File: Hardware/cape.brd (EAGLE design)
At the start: 118.2 x 97.2 mm, 48 parts, among them IC1 RT7258, IC3 74HC125, IC4 74VHC541, IC5 74VHC541, J1 FCI-10118064-5001310LF, J2 FCI-10118064-5001310LF, Q1 FDS6670, X1 RJ45-6L2-B, X2 RJ45-6L2-B

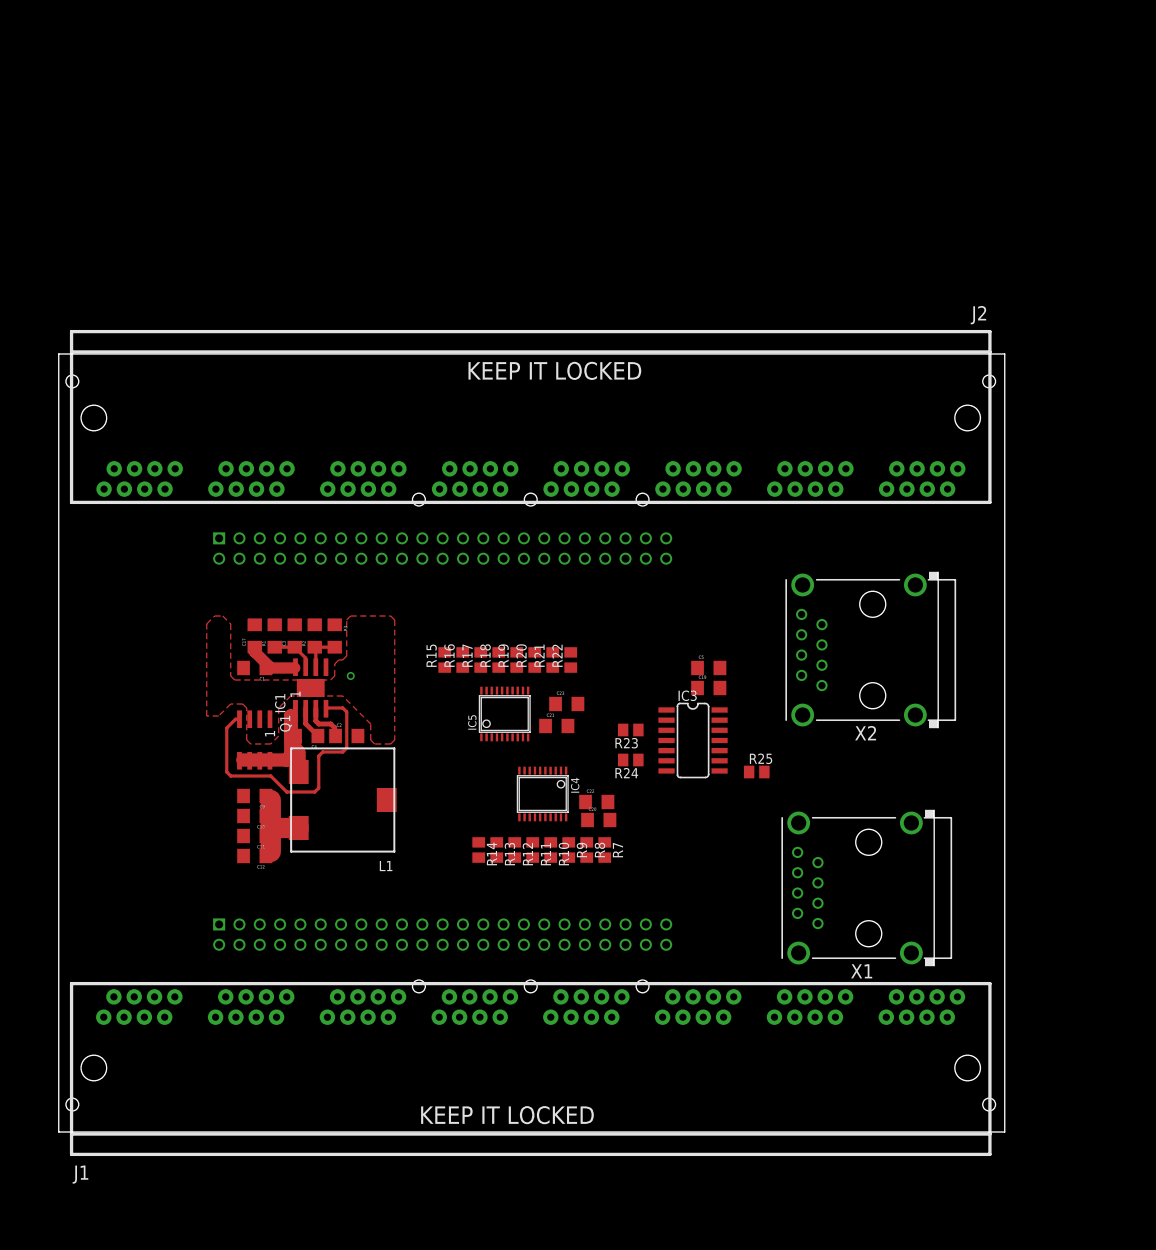
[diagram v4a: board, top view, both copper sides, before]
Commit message: Working on board routing
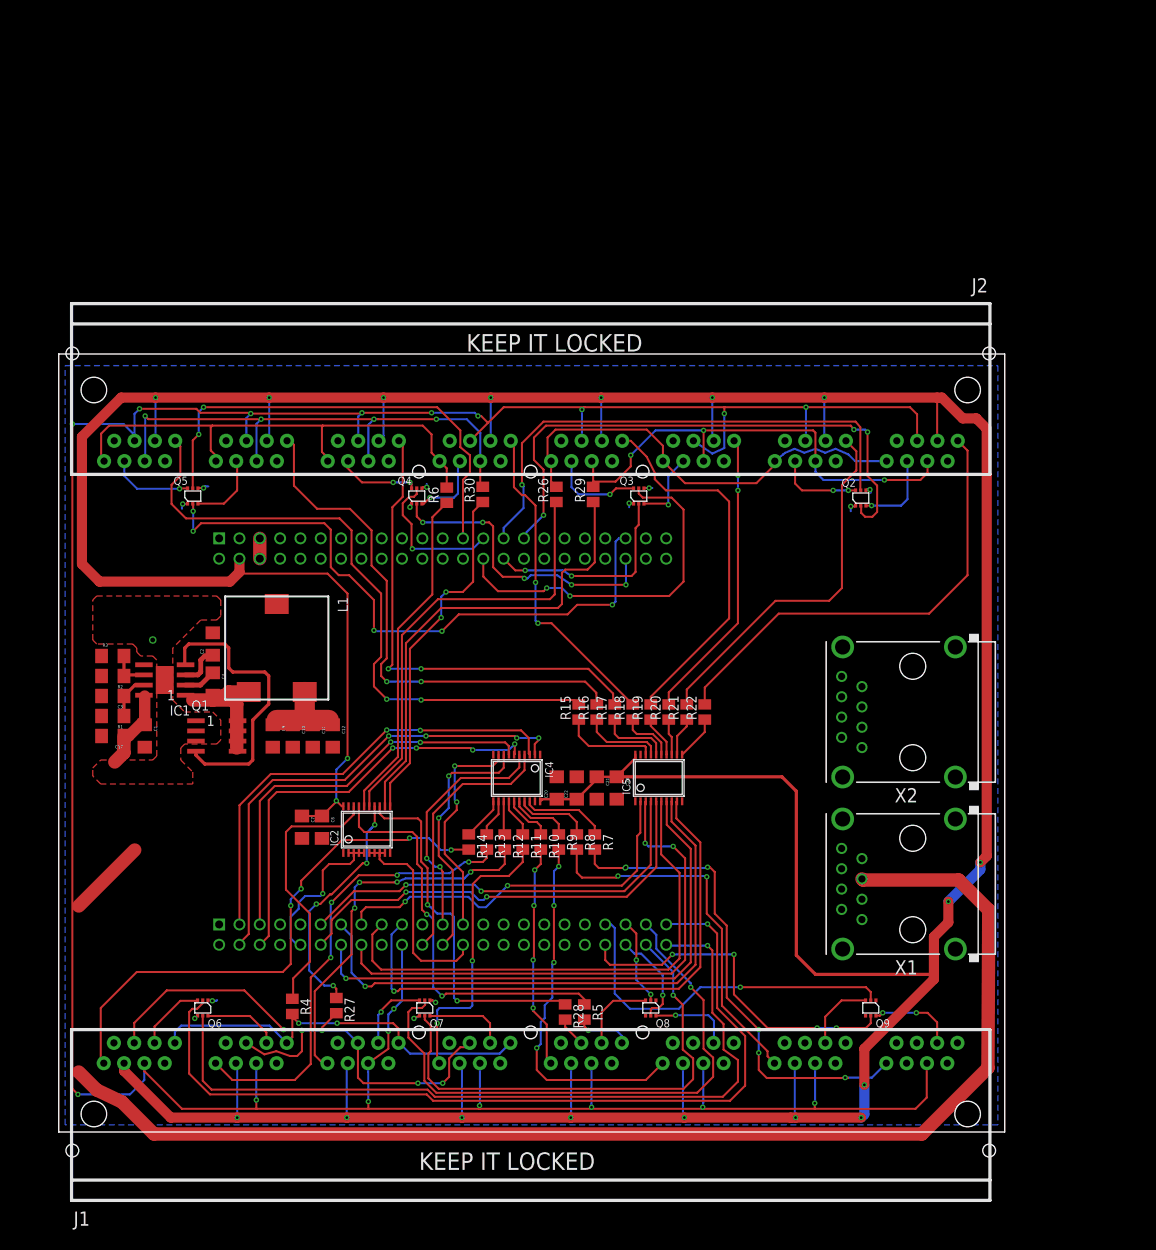
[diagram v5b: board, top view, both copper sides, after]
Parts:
- removed C19: 1uF, SparkFun-Capacitors:1206
- removed C5: 10uF, SparkFun-Capacitors:1206
- removed IC3: 74HC125, TotU:SOIC-14
- removed R23, R24, R25: (no value), resistor:M0805
- added C6: 1uF, SparkFun-Capacitors:1206
- added C7: 10uF, SparkFun-Capacitors:1206
- added IC2: 74VHC541, cape:TSSOP20
- added Q2, Q3, Q4, Q5, Q6, Q7, Q8, Q9: N-MOSFET-DUAL, cape:TSSOP6
- added R26, R27, R28, R29, R30, R4, R5, R6: (no value), resistor:M0805
- moved R3 27.9 mm to (6.75, 40.0), turned to 0 degrees
- moved R2 25.7 mm to (6.75, 37.5), turned to 180 degrees
- moved C3 24.0 mm to (6.75, 35.0), turned to 180 degrees
- moved R1 22.6 mm to (6.75, 32.5), turned to 180 degrees
- moved C17 21.7 mm to (6.75, 30.0), turned to 180 degrees
- moved IC5 20.8 mm to (75.0, 24.8)
- moved L1 20.7 mm to (27.2, 41.0), turned to 270 degrees
- moved C2 20.3 mm to (19.2, 41.5), turned to 90 degrees
- moved IC1 18.3 mm to (13.2, 37.0), turned to 90 degrees
- moved R15 18.0 mm to (65.0, 33.0)
- moved R16 18.0 mm to (67.2, 33.0)
- moved R17 18.0 mm to (69.5, 33.0)
- moved R18 18.0 mm to (71.8, 33.0)
- moved R19 18.0 mm to (74.0, 33.0)
- moved R20 18.0 mm to (76.2, 33.0)
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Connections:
- removed net BKL0: J1.A6
- removed net BLK1: J1.B6
- removed net BLK10: J2.C6
- removed net BLK11: J2.D6
- removed net BLK12: J2.E6
- removed net BLK13: J2.F6
- removed net BLK14: J2.G6
- removed net BLK15: J2.H6
- removed net BLK2: J1.C6
- removed net BLK3: J1.D6
- removed net BLK4: J1.E6
- removed net BLK5: J1.F6
- removed net BLK6: J1.G6
- removed net BLK7: J1.H6
- removed net BLK8: J2.A6
- removed net BLK9: J2.B6
- removed net DC: J1.A4, J1.B4, J1.C4, J1.D4, J1.E4, J1.F4, J1.G4, J1.H4, J2.A4, J2.B4, J2.C4, J2.D4, J2.E4, J2.F4, J2.G4, J2.H4, R24.2
- removed net N$29: IC3.8, R25.1
- removed net N$30: IC3.6, R24.1
- removed net N$31: IC3.3, R23.1
- removed net RST_RAW: IC3.9, U$1.20
- removed net SCK: J1.A8, J1.B8, J1.C8, J1.D8, J1.E8, J1.F8, J1.G8, J1.H8, J2.A8, J2.B8, J2.C8, J2.D8, J2.E8, J2.F8, J2.G8, J2.H8, R23.2
- removed net VDD_5V: U$1.52
- new net BL0: J1.A6, Q6.3
- new net BL1: J1.B6, Q6.6
- new net BL10: J2.C6, Q3.3
- new net BL11: J2.D6, Q3.6
- new net BL12: J2.E6, Q4.3
- new net BL13: J2.F6, Q4.6
- new net BL14: J2.G6, Q5.3
- new net BL15: J2.H6, Q5.6
- new net BL2: J1.C6, Q7.3
- new net BL3: J1.D6, Q7.6
- new net BL4: J1.E6, Q8.3
- new net BL5: J1.F6, Q8.6
- new net BL6: J1.G6, Q9.3
- new net BL7: J1.H6, Q9.6
- new net BL8: J2.A6, Q2.3
- new net BL9: J2.B6, Q2.6
- new net DC0: J1.A4, J1.B4, J1.C4, J1.D4, R27.2
- new net DC1: J1.E4, J1.F4, J1.G4, J1.H4, R28.2
- new net DC2: J2.A4, J2.B4, J2.C4, J2.D4, R29.2
- new net DC3: J2.E4, J2.F4, J2.G4, J2.H4, R30.2
- new net N$10: IC2.17, R5.1
- new net N$11: IC2.16, R6.1
- new net N$12: IC2.15, R26.1
- new net N$14: IC2.14, R27.1
- new net N$15: IC2.13, R28.1
- new net N$32: IC2.12, R29.1
- new net N$33: IC2.11, R30.1
- new net N$9: IC2.18, R4.1
- new net PRU0-0: Q2.2, U$1.77
- new net PRU0-1: Q2.5, U$1.75
- new net PRU0-2: Q3.2, U$1.76
- new net PRU0-3: Q3.5, U$1.74
- new net PRU0-4: Q4.2, U$1.88
- new net PRU0-5: Q4.5, U$1.73
- new net PRU0-6: Q5.2, U$1.87
- new net PRU0-7: Q5.5, U$1.71
- new net PRU1-0: Q6.2, U$1.45
- new net PRU1-1: Q6.5, U$1.46
- new net PRU1-10: U$1.28
- new net PRU1-12: U$1.21
- new net PRU1-2: Q7.2, U$1.43
- new net PRU1-3: Q7.5, U$1.44
- new net PRU1-4: Q8.2, U$1.41
- new net PRU1-5: Q8.5, U$1.42
- new net PRU1-6: Q9.2, U$1.39
- new net PRU1-7: Q9.5, U$1.40
- new net PRU1-8: U$1.27
- new net PRU1-9: U$1.29
- new net SCK0: J1.A8, J1.B8, J1.C8, J1.D8, R4.2
- new net SCK1: J1.E8, J1.F8, J1.G8, J1.H8, R5.2
- new net SCK2: J2.A8, J2.B8, J2.C8, J2.D8, R26.2
- new net SCK3: J2.E8, J2.F8, J2.G8, J2.H8, R6.2
- net DC_RAW: now also IC2.6, IC2.7, IC2.8, IC2.9; no longer IC3.5
- net GND: now also C6.2, C7.2, IC2.1, IC2.10, IC2.19, Q2.1, Q2.4, Q3.1, Q3.4, Q4.1, Q4.4, Q5.1, Q5.4, Q6.1, Q6.4, Q7.1, Q7.4, Q8.1, Q8.4, Q9.1, Q9.4; no longer C19.1, C5.1, IC3.1, IC3.10, IC3.12, IC3.13, IC3.4, IC3.7
- net RST: now also U$1.20; no longer R25.2
- net SCL_RAW: now also IC2.2, IC2.3, IC2.4, IC2.5; no longer IC3.2
- net VCC3V3: now also C6.1, C7.1, IC2.20; no longer C19.2, C5.2, IC3.14
- net VCC5V: now also U$1.52
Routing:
- net VCC3V3: track 0.00 -> 552.8 mm, vias 0 -> 19
- net RST: track 0.00 -> 396.5 mm, vias 0 -> 18
- net VIN: track 8.54 -> 179.4 mm
- net PRU1-0: track 0.00 -> 109.2 mm, vias 0 -> 1
- net PRU1-1: track 0.00 -> 100.6 mm, vias 0 -> 1
- net DATA15: track 0.00 -> 80.4 mm, vias 0 -> 2
- net PRU0-6: track 0.00 -> 77.7 mm, vias 0 -> 5
- net AD9: track 0.00 -> 73.1 mm, vias 0 -> 1
- net PRU1-2: track 0.00 -> 72.7 mm, vias 0 -> 1
- net PRU0-0: track 0.00 -> 70.7 mm, vias 0 -> 3
- net AD8: track 0.00 -> 70.6 mm, vias 0 -> 1
- net DC0: track 0.00 -> 70.2 mm, vias 0 -> 5
- net AD10: track 0.00 -> 69.8 mm, vias 0 -> 1
- net DATA0: track 0.00 -> 67.8 mm, vias 0 -> 4
- net AD14: track 0.00 -> 67.8 mm, vias 0 -> 2
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- added copper zone on layer 16, net GND

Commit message: Routing
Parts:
- removed X1, X2: RJ45-6L2-B, con-tycoelectronics:RJ45-SHIELD2
- added J3, J4: RJ45-8P8C, cape:54602-908LF
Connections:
- removed net RX+: X1.3, X2.3
- removed net RX-: X1.6, X2.6
- removed net TX+: X1.1, X2.1
- removed net TX-: X1.2, X2.2
- new net RX_N: J3.6, J4.6
- new net RX_P: J3.3, J4.3
- new net TX_N: J3.2, J4.2
- new net TX_P: J3.1, J4.1
- net GND: now also J3.7, J3.8; no longer X1.7, X1.8, X1.S1, X1.S2, X1.S3, X1.S4, X2.S1, X2.S2, X2.S3, X2.S4
- net VIN: now also J3.4, J3.5; no longer X1.4, X1.5
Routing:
- net DC1: track 3.74 -> 62.4 mm, vias 0 -> 2
- net VCC5V: track 18.5 -> 75.3 mm, vias 0 -> 3
- net GND: track 13.0 -> 68.8 mm, vias 13 -> 231
- net SCK1: track 6.91 -> 55.9 mm, vias 1 -> 2
- net TX_P: track 0.00 -> 37.4 mm
- net VIN: track 179.4 -> 212.7 mm, vias 0 -> 1
- net RX_N: track 0.00 -> 30.4 mm
- net TX_N: track 0.00 -> 29.6 mm
- net RX_P: track 0.00 -> 27.1 mm
- net VCC3V3: track 552.8 -> 561.5 mm
- net DC0: track 70.2 -> 67.3 mm, vias 5 -> 4
- net DATA7: track 62.3 -> 61.6 mm, vias 6 -> 5
- net N$4: track 21.8 -> 22.3 mm
- net BL5: track 10.3 -> 10.1 mm, vias 1 -> 2
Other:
- board size 118.2 x 97.2 mm -> 118.2 x 103.5 mm

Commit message: Finished v1 board
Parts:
- added 3V, 5V, GND, PRU1-10, PRU1-12, PRU1-8, PRU1-9, VIN: PTR1TP20R, tenna_avr_AD7021_v0_9_shrink:TP20R
- added F1: PTC, cape:LF-1812L
- added U$2, U$3: (no value), holes:3,2
- added U$4, U$5, U$6: FIDUCIAL, adafruit:FIDUCIAL_1MM
- L1: value MURATA_INDUCTOR_3900 -> 2.8uH
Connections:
- new net VFUSE: C1.1, C17.1, F1.P$1C, IC1.8, R1.2
- net GND: now also GND.TP
- net PRU1-10: now also PRU1-10.TP
- net PRU1-12: now also PRU1-12.TP
- net PRU1-8: now also PRU1-8.TP
- net PRU1-9: now also PRU1-9.TP
- net VCC3V3: now also 3V.TP
- net VCC5V: now also 5V.TP
- net VIN: now also F1.P$2, VIN.TP; no longer C1.1, C17.1, IC1.8, R1.2
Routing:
- net VIN: track 212.7 -> 174.4 mm
- net VFUSE: track 0.00 -> 37.8 mm
- net VCC5V: track 75.3 -> 94.2 mm
- net PRU1-12: track 0.00 -> 10.2 mm
- net PRU1-9: track 0.00 -> 4.78 mm
- net PRU1-8: track 0.00 -> 3.89 mm
- net DATA0: track 67.8 -> 71.3 mm
- net PRU1-10: track 0.00 -> 3.26 mm
- net VCC3V3: track 561.5 -> 564.1 mm
- net GND: track 68.8 -> 70.4 mm
- net DC0: track 67.3 -> 65.8 mm
- net AD13: track 52.9 -> 54.0 mm
- net AD15: track 48.1 -> 49.0 mm
- net DATA4: track 28.0 -> 28.7 mm
- net BL0: track 8.77 -> 8.06 mm
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
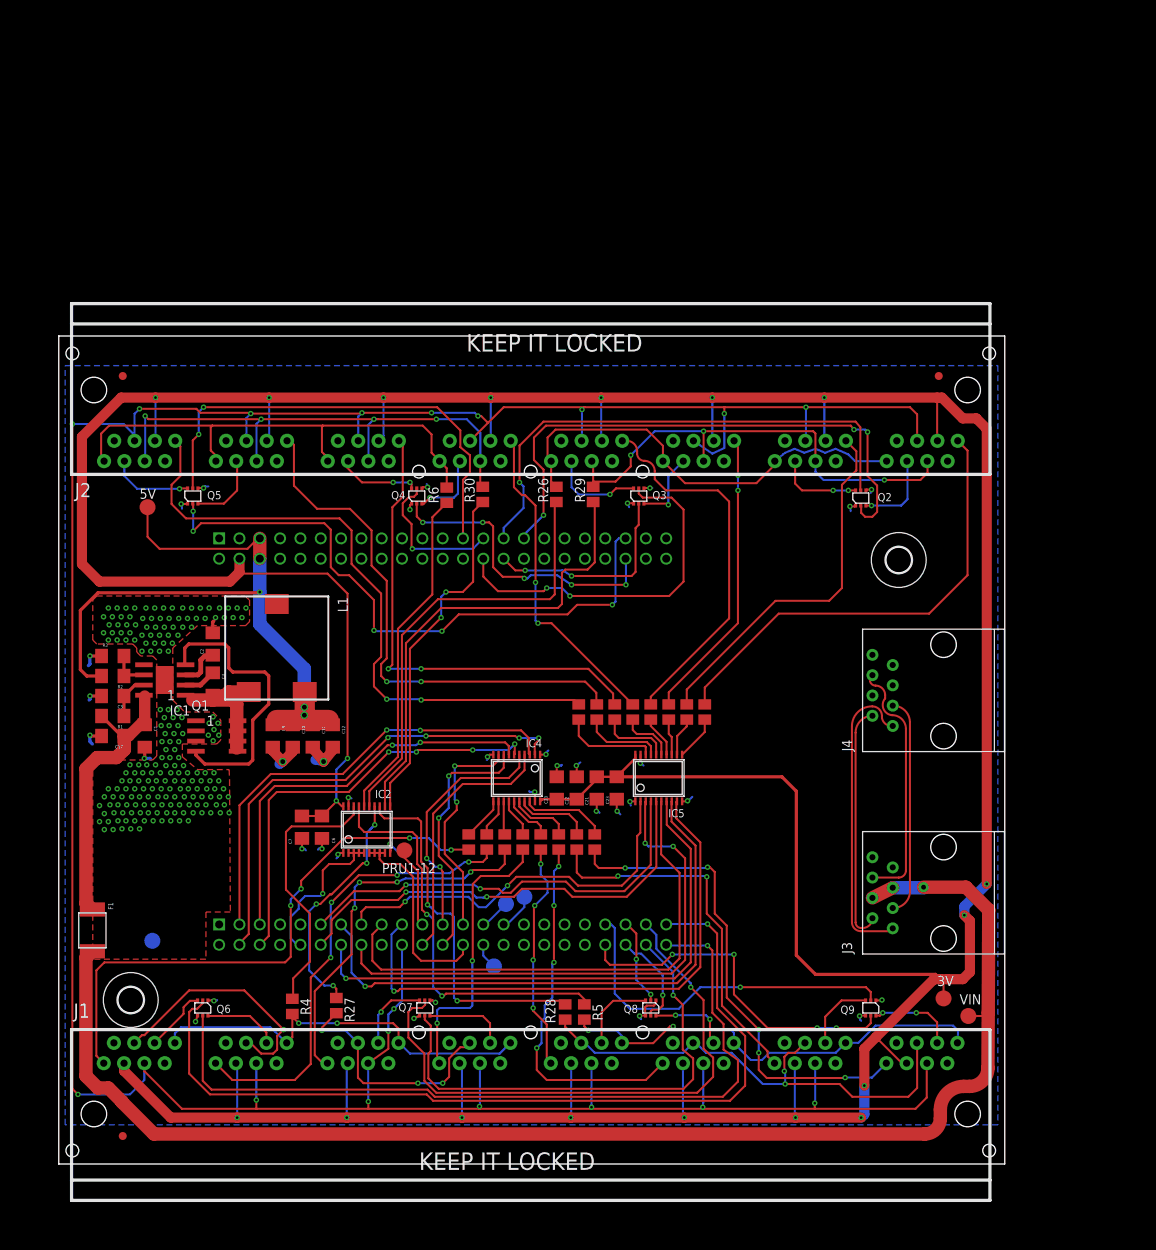
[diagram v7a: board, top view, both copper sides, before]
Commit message: added bird and fixed dimensions
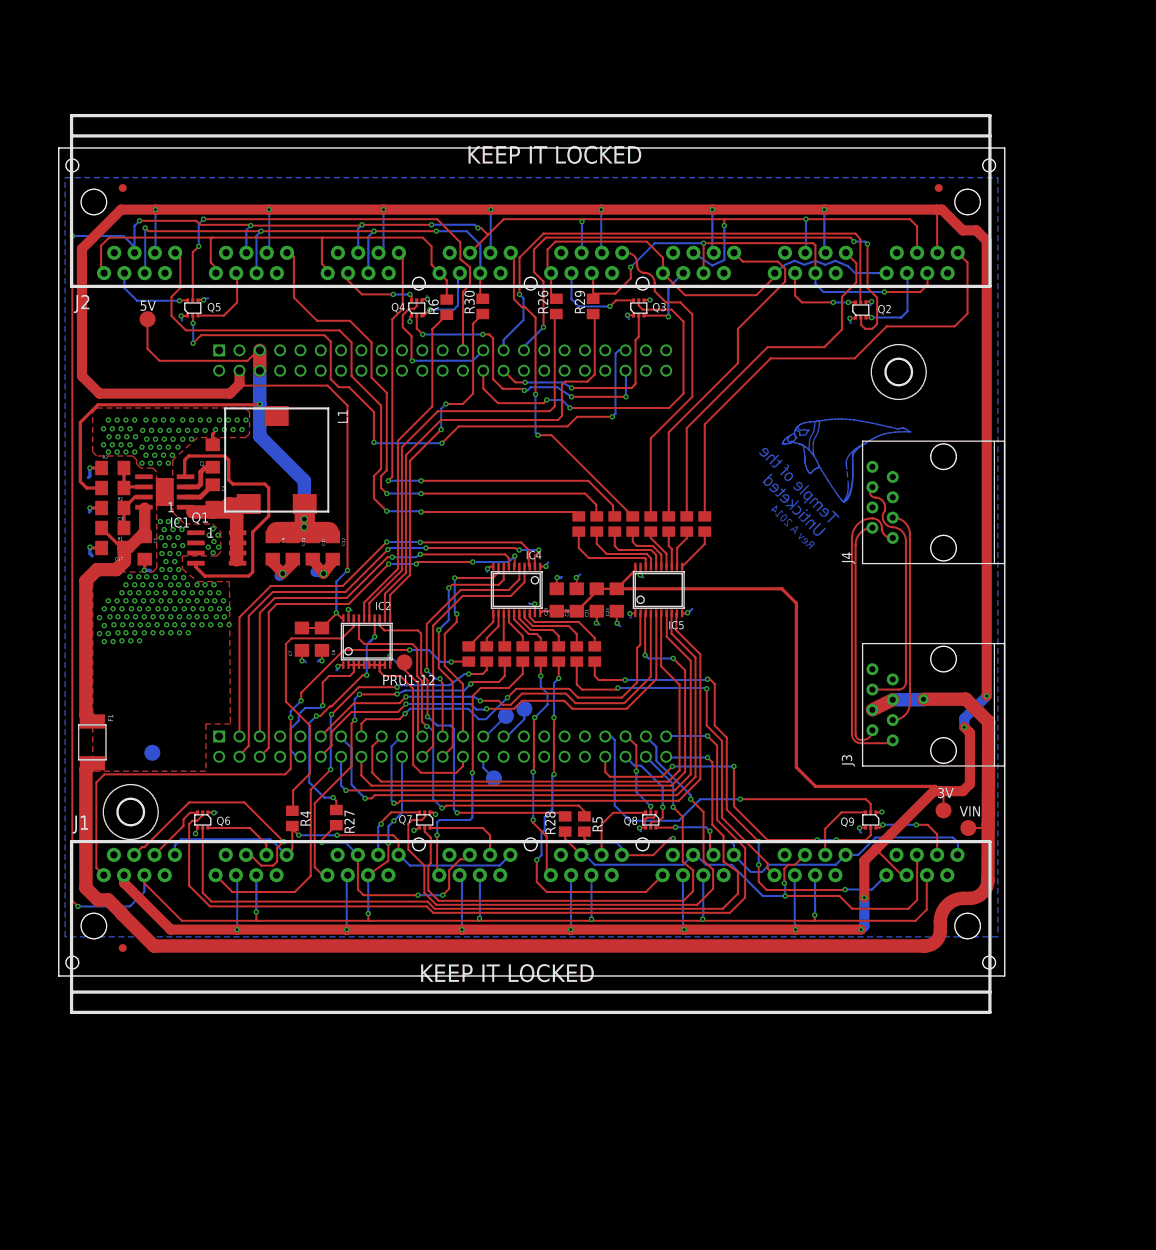
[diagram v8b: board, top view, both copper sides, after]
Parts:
- moved PRU1-12 23.5 mm to (43.2, 39.2)
- moved 3V 23.5 mm to (110.6, 20.7)
- moved C1 23.5 mm to (10.8, 53.5)
- moved C10 23.5 mm to (29.2, 53.5)
- moved C11 23.5 mm to (31.8, 53.5)
- moved C12 23.5 mm to (34.2, 53.5)
- moved C17 23.5 mm to (6.75, 53.5)
- moved C2 23.5 mm to (19.2, 65.0)
- moved C20 23.5 mm to (62.2, 47.0)
- moved C21 23.5 mm to (67.2, 47.0)
- moved C22 23.5 mm to (64.8, 47.0)
- moved C23 23.5 mm to (69.8, 47.0)
- moved C3 23.5 mm to (6.75, 58.5)
- moved C4 23.5 mm to (19.2, 60.0)
- moved C6 23.5 mm to (32.9, 42.1)
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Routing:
- net BIRD1: track 0.00 -> 50.8 mm
- net DATA10: track 36.7 -> 44.2 mm, vias 2 -> 0
- net DATA11: track 46.7 -> 40.1 mm
- added copper zone on layer 16, net BIRD1
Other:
- board text added: "Rev A 2014"
- board text added: "Temple of the Unticketed"
